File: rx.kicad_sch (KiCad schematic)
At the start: 19 parts, among them P1 SMA, U11 SKY65404, U9 TRF37A73

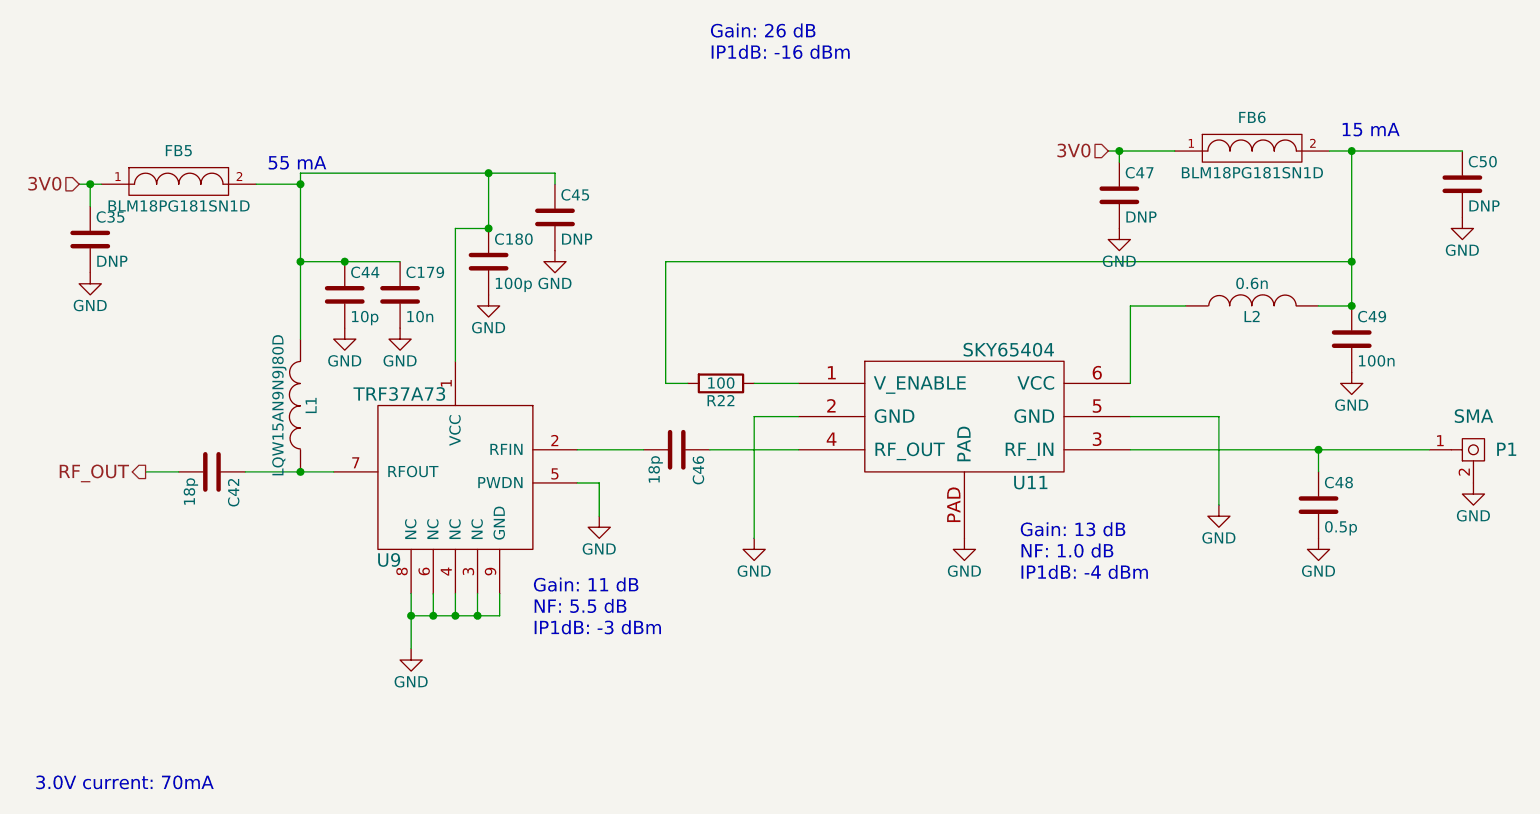
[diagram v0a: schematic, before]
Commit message: DNP components are deleted
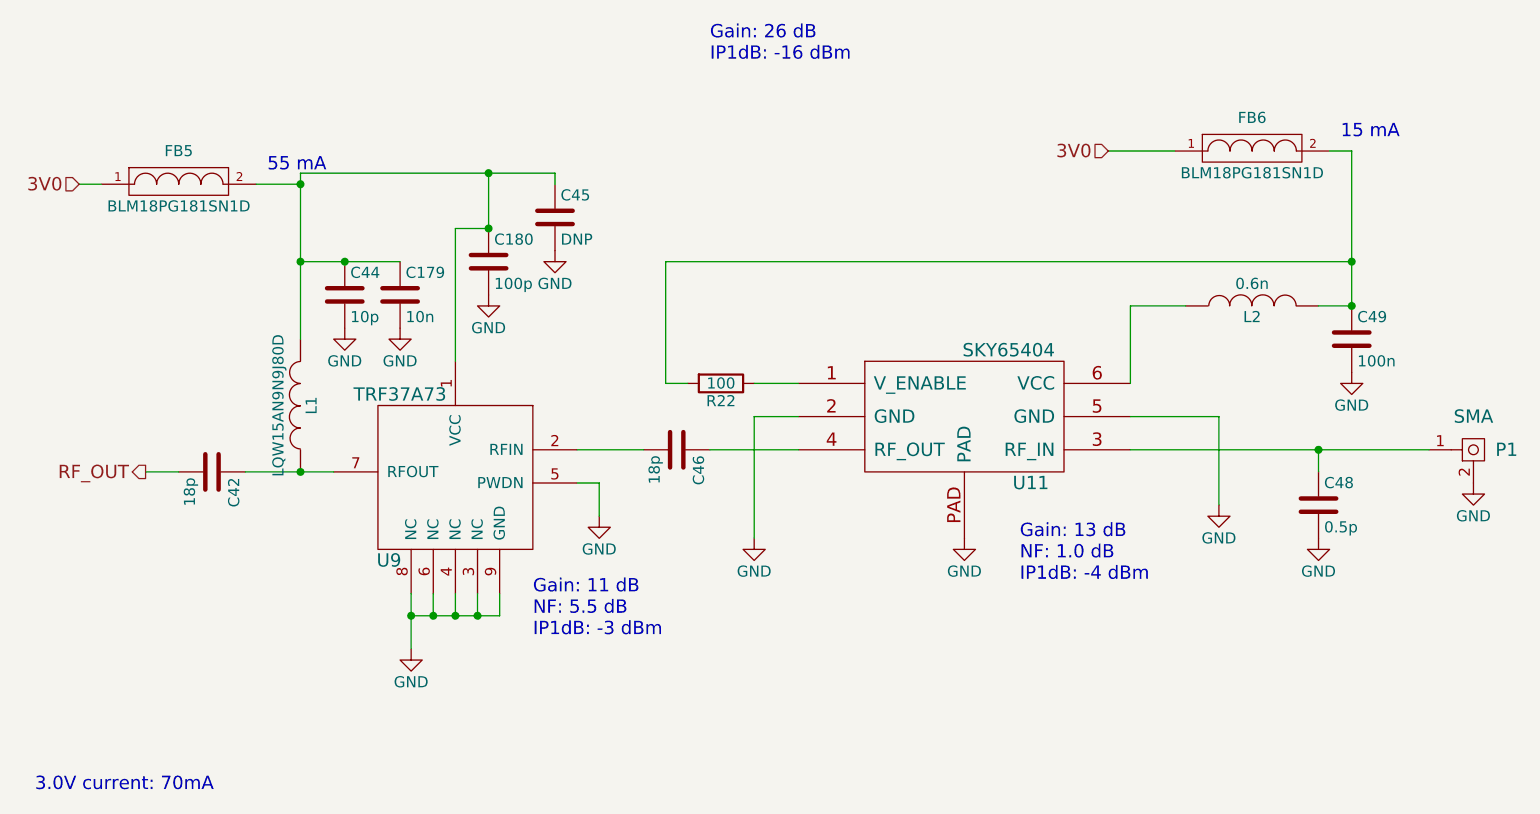
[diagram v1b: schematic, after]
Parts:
- removed C35, C47, C50: DNP, Footprints:SMD_0603, symbol fmcw3-rescue:C

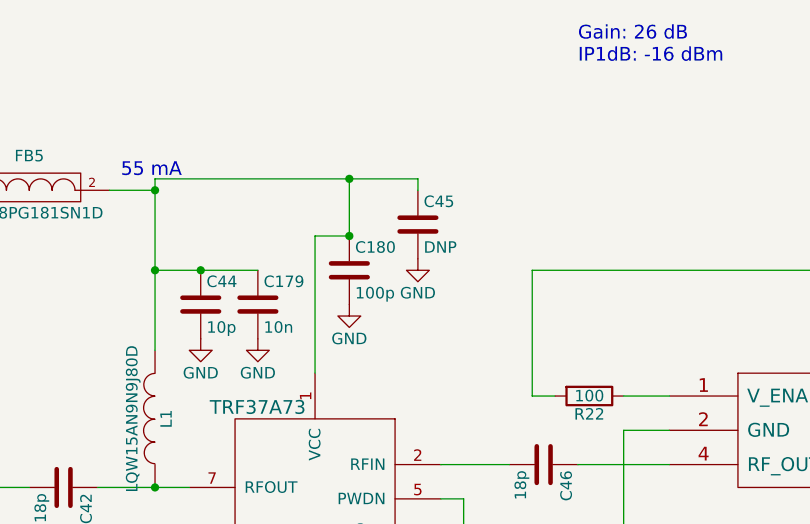
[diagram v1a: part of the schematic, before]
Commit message: pcb is checked dnp is deleted copper pours are checked
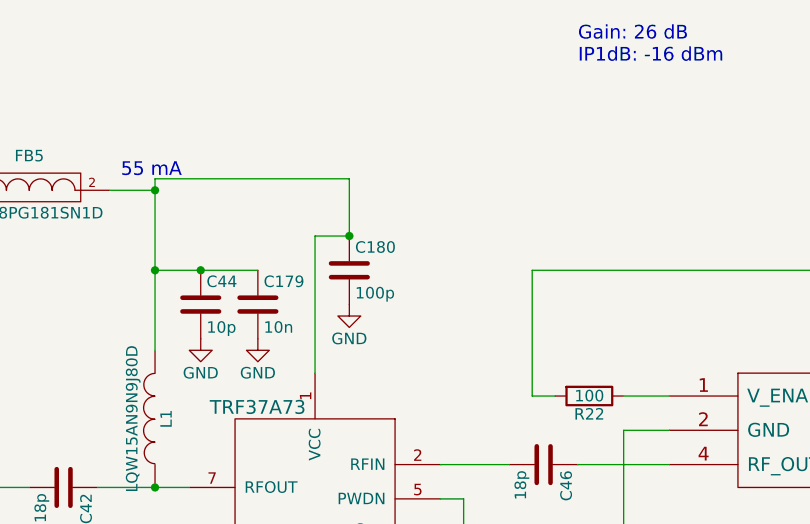
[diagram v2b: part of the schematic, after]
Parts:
- removed C45: DNP, Footprints:SMD_0603, symbol fmcw3-rescue:C
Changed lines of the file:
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@@
-	)
-	(junction
-		(at 119.38 68.58)
-		(diameter 0)
-		(color 0 0 0 0)
 	)
 	(junction
@@
 	(wire
 		(pts
-			(xy 127 68.58) (xy 119.38 68.58)
-		)
-		(stroke
-			(width 0)
-			(type default)
-		)
-	)
-	(wire
-		(pts
 			(xy 110.49 116.84) (xy 110.49 119.38)
 		)
@@
 		(pts
 			(xy 118.11 119.38) (xy 120.65 119.38)
-		)
-		(stroke
-			(width 0)
-			(type default)
-		)
-	)
-	(wire
-		(pts
-			(xy 127 69.85) (xy 127 68.58)
 		)
 		(stroke
@@
 					(unit 1)
 				)
-			)
-		)
-	)
-	(symbol
-		(lib_id "fmcw3-rescue:C")
-		(at 127 73.66 0)
-		(unit 1)
-		(exclude_from_sim no)
-		(in_bom yes)
-		(on_board yes)
-		(dnp no)
-		(property "Reference" "C45"
-			(at 127.635 71.12 0)
-			(effects
-				(font
-					(size 1.27 1.27)
-				)
-				(justify left)
-			)
-		)
-		(property "Value" "DNP"
-			(at 127.635 76.2 0)
-			(effects
-				(font
-					(size 1.27 1.27)
-				)
-				(justify left)
-			)
-		)
-		(property "Footprint" "Footprints:SMD_0603"
-			(at 127.9652 77.47 0)
-			(effects
-				(font
-					(size 0.762 0.762)
-				)
-				(hide yes)
-			)
-		)
-		(property "Datasheet" ""
-			(at 127 73.66 0)
-			(effects
-				(font
-					(size 1.524 1.524)
-				)
-			)
-		)
-		(property "Description" ""
-			(at 127 73.66 0)
-			(effects
-				(font
-					(size 1.27 1.27)
-				)
-			)
-		)
-		(pin "1"
-		)
-		(pin "2"
-		)
-		(instances
-			(project "fmcw3"
-				(path "/25ababa6-1178-4b22-9ad6-058222120a27/00000000-0000-0000-0000-000059396b97"
-					(reference "C45")
-					(unit 1)
-				)
-				(path "/25ababa6-1178-4b22-9ad6-058222120a27/00000000-0000-0000-0000-0000593d90ba"
-					(reference "C54")
-					(unit 1)
-				)
-			)
-		)
-	)
-	(symbol
-		(lib_id "fmcw3-rescue:GND")
-		(at 127 77.47 0)
-		(unit 1)
-		(exclude_from_sim no)
-		(in_bom yes)
-		(on_board yes)
-		(dnp no)
-		(property "Reference" "#PWR0142"
-			(at 127 83.82 0)
-			(effects
-				(font
-					(size 1.27 1.27)
-				)
-				(hide yes)
-			)
-		)
-		(property "Value" "GND"
-			(at 127 81.28 0)
-			(effects
-				(font
-					(size 1.27 1.27)
-				)
-			)
-		)
-		(property "Footprint" ""
-			(at 127 77.47 0)
-			(effects
-				(font
-					(size 1.524 1.524)
-				)
-			)
-		)
-		(property "Datasheet" ""
-			(at 127 77.47 0)
-			(effects
-				(font
-					(size 1.524 1.524)
-				)
-			)
-		)
-		(property "Description" ""
-			(at 127 77.47 0)
-			(effects
-				(font
-					(size 1.27 1.27)
-				)
-			)
-		)
-		(pin "1"
-		)
-		(instances
-			(project "fmcw3"
-				(path "/25ababa6-1178-4b22-9ad6-058222120a27/00000000-0000-0000-0000-000059396b97"
-					(reference "#PWR0142")
-					(unit 1)
-				)
-				(path "/25ababa6-1178-4b22-9ad6-058222120a27/00000000-0000-0000-0000-0000593d90ba"
-					(reference "#PWR0109")
-					(unit 1)
-				)
